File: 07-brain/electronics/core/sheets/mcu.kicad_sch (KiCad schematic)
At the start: 0 parts

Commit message: Added audio io to Brain
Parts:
- added U9: Pico, RPi_Pico:RPi_Pico_SMD_TH, symbol MCU_RaspberryPi_and_Boards:Pico
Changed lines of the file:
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@@
 	(generator_version "9.0")
 	(paper "A4")
+	(symbol
+		(lib_id "MCU_RaspberryPi_and_Boards:Pico")
+		(at 148.59 78.74 0)
+		(unit 1)
+		(exclude_from_sim no)
+		(in_bom yes)
+		(on_board yes)
+		(dnp no)
+		(fields_autoplaced yes)
+		(property "Reference" "U9"
+			(at 148.59 46.99 0)
+			(effects
+				(font
+					(size 1.27 1.27)
+				)
+			)
+		)
+		(property "Value" "Pico"
+			(at 148.59 49.53 0)
+			(effects
+				(font
+					(size 1.27 1.27)
+				)
+			)
+		)
+		(property "Footprint" "RPi_Pico:RPi_Pico_SMD_TH"
+			(at 148.59 78.74 90)
+			(effects
+				(font
+					(size 1.27 1.27)
+				)
+				(hide yes)
+			)
+		)
+		(property "Datasheet" ""
+			(at 148.59 78.74 0)
+			(effects
+				(font
+					(size 1.27 1.27)
+				)
+				(hide yes)
+			)
+		)
+		(property "Description" ""
+			(at 148.59 78.74 0)
+			(effects
+				(font
+					(size 1.27 1.27)
+				)
+				(hide yes)
+			)
+		)
+		(pin "4"
+		)
+		(pin "5"
+		)
+		(pin "6"
+		)
+		(pin "7"
+		)
+		(pin "8"
+		)
+		(pin "42"
+		)
+		(pin "43"
+		)
+		(pin "40"
+		)
+		(pin "39"
+		)
+		(pin "9"
+		)
+		(pin "38"
+		)
+		(pin "37"
+		)
+		(pin "36"
+		)
+		(pin "35"
+		)
+		(pin "34"
+		)
+		(pin "33"
+		)
+		(pin "32"
+		)
+		(pin "31"
+		)
+		(pin "10"
+		)
+		(pin "11"
+		)
+		(pin "12"
+		)
+		(pin "13"
+		)
+		(pin "14"
+		)
+		(pin "15"
+		)
+		(pin "16"
+		)
+		(pin "17"
+		)
+		(pin "18"
+		)
+		(pin "19"
+		)
+		(pin "20"
+		)
+		(pin "41"
+		)
+		(pin "30"
+		)
+		(pin "29"
+		)
+		(pin "28"
+		)
+		(pin "27"
+		)
+		(pin "26"
+		)
+		(pin "25"
+		)
+		(pin "24"
+		)
+		(pin "23"
+		)
+		(pin "22"
+		)
+		(pin "21"
+		)
+		(pin "1"
+		)
+		(pin "2"
+		)
+		(pin "3"
+		)
+		(instances
+			(project ""
+				(path "/8e2e31f3-eed5-4de1-966c-f4162758c735/e381105c-725b-4f82-965a-3ba61dbc8b0a"
+					(reference "U9")
+					(unit 1)
+				)
+			)
+		)
+	)
 )

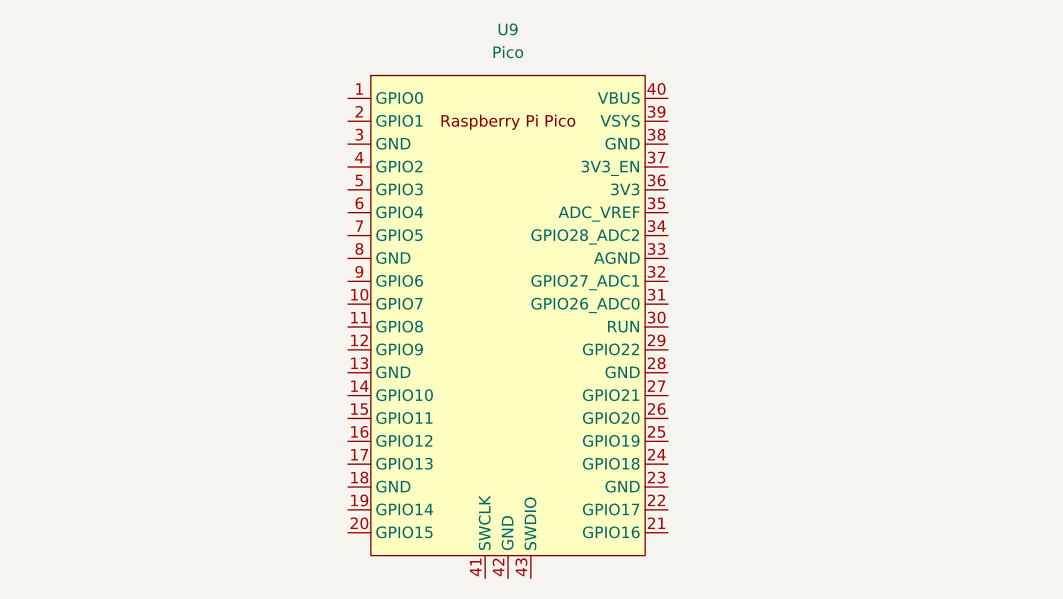
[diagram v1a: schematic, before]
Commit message: Added LED component to Brain (untested)
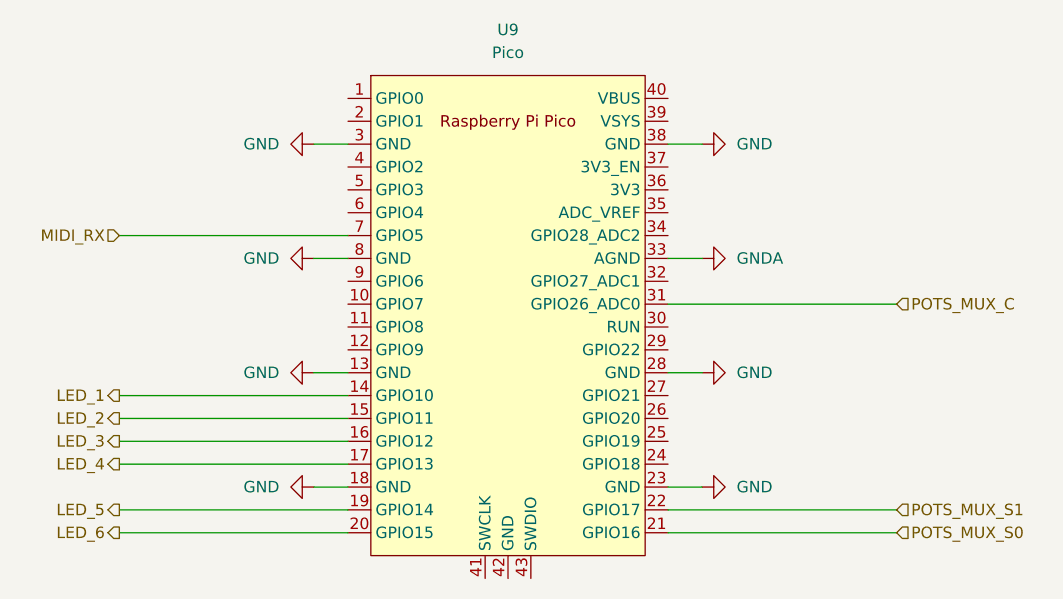
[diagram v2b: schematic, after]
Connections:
- net GND: now reaches U9.13 (GND)
- net GND: now also U9.18 (GND), U9.23 (GND), U9.28 (GND), U9.3 (GND), U9.38 (GND), U9.8 (GND)
- net LED_1: now reaches U9.14 (GPIO10)
- net LED_2: now reaches U9.15 (GPIO11)
- net LED_3: now reaches U9.16 (GPIO12)
- net LED_4: now reaches U9.17 (GPIO13)
- net LED_5: now reaches U9.19 (GPIO14)
- net LED_6: now reaches U9.20 (GPIO15)
- net POTS_MUX_S0: now reaches U9.21 (GPIO16)
- net POTS_MUX_S1: now reaches U9.22 (GPIO17)
- net POTS_MUX_C: now reaches U9.31 (GPIO26_ADC0)
- net GNDA: now reaches U9.33 (AGND)
- net MIDI_RX: now reaches U9.7 (GPIO5)

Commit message: Updated Brain schematics
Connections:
- net GND: now also U9.42 (GND)
- net MIDI_RX: now also U9.12 (GPIO9); no longer U9.7 (GPIO5)
- net UART_TX: now reaches U9.1 (GPIO0)
- net OUT_COUPLING_S2: now reaches U9.10 (GPIO7)
- net GPIO_PULSE_OUT: now reaches U9.11 (GPIO8)
- net UART_RX: now reaches U9.2 (GPIO1)
- net BTN_1: now reaches U9.24 (GPIO18)
- net BTN_2: now reaches U9.25 (GPIO19)
- net BTN_1_LED: now reaches U9.26 (GPIO20)
- net BTN_2_LED: now reaches U9.27 (GPIO21)
- net GPIO_AUDIO_IN_1: now reaches U9.32 (GPIO27_ADC1)
- net GPIO_AUDIO_IN_2: now reaches U9.34 (GPIO28_ADC2)
- net +3.3V: now reaches U9.36 (3V3)
- net +5V: now reaches U9.39 (VSYS)
- net DAC_SCK: now reaches U9.4 (GPIO2)
- net SWCLK: now reaches U9.41 (SWCLK)
- net SWDIO: now reaches U9.43 (SWDIO)
- net GPIO_PULSE_IN: now reaches U9.5 (GPIO3)
- net DAC_SDI: now reaches U9.6 (GPIO4)
- net OUT_COUPLING_S1: now reaches U9.9 (GPIO6)
- new net DAC_CS: U9.7 (GPIO5)
- no-connect marks 0 -> 5

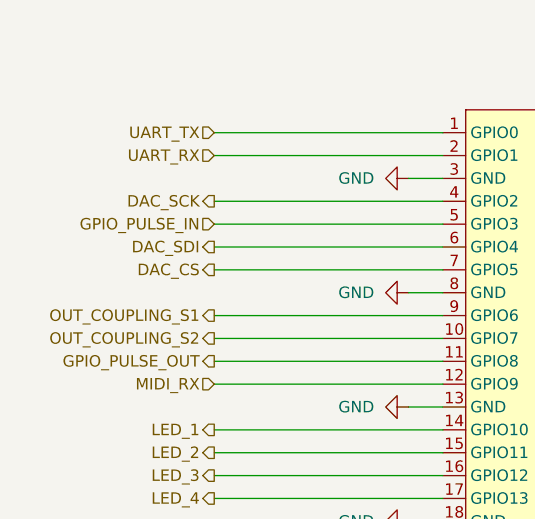
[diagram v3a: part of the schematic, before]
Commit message: Fixed DAC SPI bug in BrainSDK
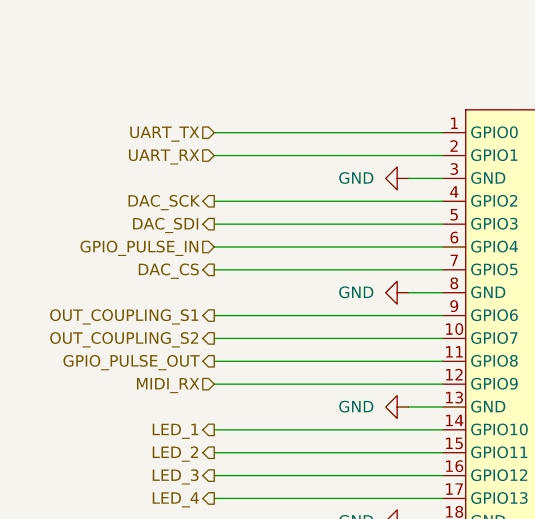
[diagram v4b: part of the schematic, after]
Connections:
- net DAC_SDI: now also U9.5 (GPIO3); no longer U9.6 (GPIO4)
- net GPIO_PULSE_IN: now also U9.6 (GPIO4); no longer U9.5 (GPIO3)
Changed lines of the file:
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@@
 	(hierarchical_label "DAC_SDI"
 		(shape output)
-		(at 105.41 67.31 180)
+		(at 105.41 64.77 180)
 		(effects
 			(font
@@
 	(hierarchical_label "GPIO_PULSE_IN"
 		(shape input)
-		(at 105.41 64.77 180)
+		(at 105.41 67.31 180)
 		(effects
 			(font

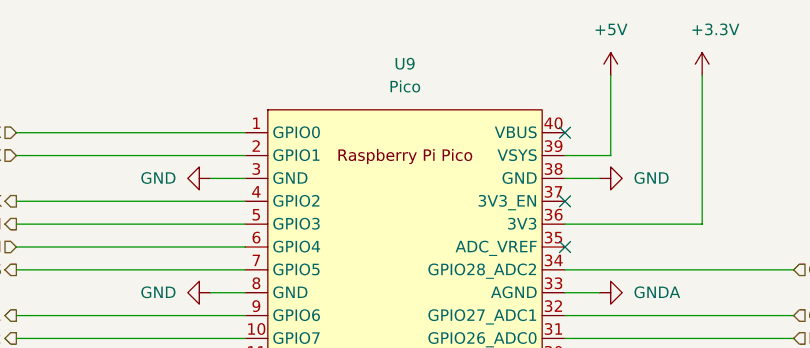
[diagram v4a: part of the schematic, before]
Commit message: Audio/CV out BrainSDK tested/working
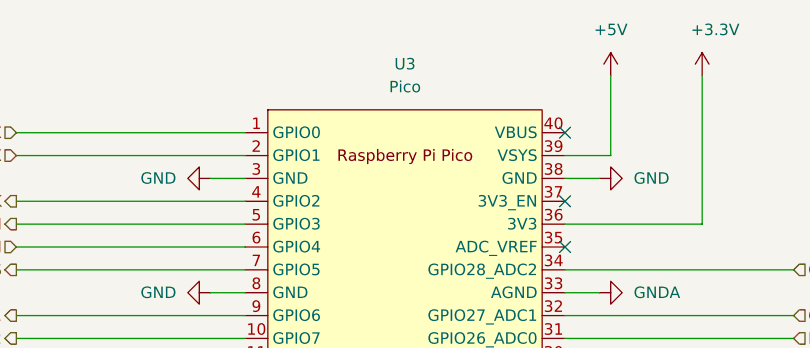
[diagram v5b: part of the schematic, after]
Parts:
- renumbered U9 to U3
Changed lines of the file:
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@@
 		(dnp no)
 		(fields_autoplaced yes)
-		(property "Reference" "#PWR080"
+		(property "Reference" "#PWR030"
 			(at 120.65 85.09 0)
 			(effects
@@
 			(project "brain-core"
 				(path "/8e2e31f3-eed5-4de1-966c-f4162758c735/e381105c-725b-4f82-965a-3ba61dbc8b0a"
-					(reference "#PWR080")
+					(reference "#PWR030")
 					(unit 1)
 				)
@@
 		(dnp no)
 		(fields_autoplaced yes)
-		(property "Reference" "#PWR079"
+		(property "Reference" "#PWR031"
 			(at 120.65 97.79 0)
 			(effects
@@
 			(project ""
 				(path "/8e2e31f3-eed5-4de1-966c-f4162758c735/e381105c-725b-4f82-965a-3ba61dbc8b0a"
-					(reference "#PWR079")
+					(reference "#PWR031")
 					(unit 1)
 				)
@@
 		(dnp no)
 		(fields_autoplaced yes)
-		(property "Reference" "#PWR083"
+		(property "Reference" "#PWR033"
 			(at 176.53 59.69 0)
 			(effects
@@
 			(project "brain-core"
 				(path "/8e2e31f3-eed5-4de1-966c-f4162758c735/e381105c-725b-4f82-965a-3ba61dbc8b0a"
-					(reference "#PWR083")
+					(reference "#PWR033")
 					(unit 1)
 				)
@@
 		(dnp no)
 		(fields_autoplaced yes)
-		(property "Reference" "#PWR082"
+		(property "Reference" "#PWR028"
 			(at 120.65 59.69 0)
 			(effects
@@
 			(project "brain-core"
 				(path "/8e2e31f3-eed5-4de1-966c-f4162758c735/e381105c-725b-4f82-965a-3ba61dbc8b0a"
-					(reference "#PWR082")
+					(reference "#PWR028")
 					(unit 1)
 				)
@@
 		(dnp no)
 		(fields_autoplaced yes)
-		(property "Reference" "#PWR081"
+		(property "Reference" "#PWR029"
 			(at 120.65 72.39 0)
 			(effects
@@
 			(project ""
 				(path "/8e2e31f3-eed5-4de1-966c-f4162758c735/e381105c-725b-4f82-965a-3ba61dbc8b0a"
-					(reference "#PWR081")
+					(reference "#PWR029")
 					(unit 1)
 				)
@@
 		(dnp no)
 		(fields_autoplaced yes)
-		(property "Reference" "#PWR076"
+		(property "Reference" "#PWR034"
 			(at 176.53 72.39 0)
 			(effects
@@
 			(project ""
 				(path "/8e2e31f3-eed5-4de1-966c-f4162758c735/e381105c-725b-4f82-965a-3ba61dbc8b0a"
-					(reference "#PWR076")
+					(reference "#PWR034")
 					(unit 1)
 				)
@@
 		(dnp no)
 		(fields_autoplaced yes)
-		(property "Reference" "U9"
+		(property "Reference" "U3"
 			(at 148.59 46.99 0)
 			(effects
@@
 			(project ""
 				(path "/8e2e31f3-eed5-4de1-966c-f4162758c735/e381105c-725b-4f82-965a-3ba61dbc8b0a"
-					(reference "U9")
+					(reference "U3")
 					(unit 1)
 				)
@@
 		(dnp no)
 		(fields_autoplaced yes)
-		(property "Reference" "#PWR077"
+		(property "Reference" "#PWR035"
 			(at 176.53 85.09 0)
 			(effects
@@
 			(project ""
 				(path "/8e2e31f3-eed5-4de1-966c-f4162758c735/e381105c-725b-4f82-965a-3ba61dbc8b0a"
-					(reference "#PWR077")
+					(reference "#PWR035")
 					(unit 1)
 				)
@@
 		(dnp no)
 		(fields_autoplaced yes)
-		(property "Reference" "#PWR031"
+		(property "Reference" "#PWR037"
 			(at 171.45 52.07 0)
 			(effects
@@
 			(project ""
 				(path "/8e2e31f3-eed5-4de1-966c-f4162758c735/e381105c-725b-4f82-965a-3ba61dbc8b0a"
-					(reference "#PWR031")
+					(reference "#PWR037")
 					(unit 1)
 				)
@@
 		(on_board yes)
 		(dnp no)
-		(property "Reference" "#PWR03"
+		(property "Reference" "#PWR038"
 			(at 181.61 52.07 0)
 			(effects
@@
 			(project ""
 				(path "/8e2e31f3-eed5-4de1-966c-f4162758c735/e381105c-725b-4f82-965a-3ba61dbc8b0a"
-					(reference "#PWR03")
+					(reference "#PWR038")
 					(unit 1)
 				)
@@
 		(dnp no)
 		(fields_autoplaced yes)
-		(property "Reference" "#PWR084"
+		(property "Reference" "#PWR032"
 			(at 148.59 123.19 0)
 			(effects
@@
 			(project ""
 				(path "/8e2e31f3-eed5-4de1-966c-f4162758c735/e381105c-725b-4f82-965a-3ba61dbc8b0a"
-					(reference "#PWR084")
+					(reference "#PWR032")
 					(unit 1)
 				)
@@
 		(dnp no)
 		(fields_autoplaced yes)
-		(property "Reference" "#PWR078"
+		(property "Reference" "#PWR036"
 			(at 176.53 97.79 0)
 			(effects
@@
 			(project "brain-core"
 				(path "/8e2e31f3-eed5-4de1-966c-f4162758c735/e381105c-725b-4f82-965a-3ba61dbc8b0a"
-					(reference "#PWR078")
-					(unit 1)
-				)
+					(reference "#PWR036")
+					(unit 1)
+				)

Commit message: Design Brain/Core PCB
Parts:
- U3: footprint RPi_Pico:RPi_Pico_SMD_TH -> Module:RaspberryPi_Pico_Common_Unspecified
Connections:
- net GND: no longer U3.42 (GND)
- net POTS_MUX_S0: now also U3.22 (GPIO17); no longer U3.21 (GPIO16)
- net POTS_MUX_S1: now also U3.21 (GPIO16); no longer U3.22 (GPIO17)
- net SWCLK: no longer names the net of U3.41 (SWCLK)
- net SWDIO: no longer names the net of U3.43 (SWDIO)
- no-connect marks 5 -> 8
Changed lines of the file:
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@@
+	)
+	(no_connect
+		(at 148.59 107.95)
 	)
 	(no_connect
@@
 		(at 166.37 80.01)
 	)
+	(no_connect
+		(at 151.13 107.95)
+	)
+	(no_connect
+		(at 146.05 107.95)
+	)
 	(wire
 		(pts
@@
 	(wire
 		(pts
-			(xy 148.59 116.84) (xy 148.59 107.95)
-		)
-		(stroke
-			(width 0)
-			(type default)
-		)
-	)
-	(wire
-		(pts
 			(xy 105.41 102.87) (xy 130.81 102.87)
 		)
@@
 		(pts
 			(xy 127 59.69) (xy 130.81 59.69)
-		)
-		(stroke
-			(width 0)
-			(type default)
-		)
-	)
-	(wire
-		(pts
-			(xy 151.13 107.95) (xy 151.13 111.76)
-		)
-		(stroke
-			(width 0)
-			(type default)
-		)
-	)
-	(wire
-		(pts
-			(xy 146.05 111.76) (xy 146.05 107.95)
 		)
 		(stroke
@@
 		)
 	)
-	(hierarchical_label "SWCLK"
-		(shape input)
-		(at 146.05 111.76 270)
-		(effects
-			(font
-				(size 1.27 1.27)
-			)
-			(justify right)
-		)
-	)
 	(hierarchical_label "BTN_2"
 		(shape input)
@@
 		)
 	)
-	(hierarchical_label "SWDIO"
-		(shape input)
-		(at 151.13 111.76 270)
-		(effects
-			(font
-				(size 1.27 1.27)
-			)
-			(justify right)
-		)
-	)
 	(hierarchical_label "LED_1"
 		(shape output)
@@
 	(hierarchical_label "POTS_MUX_S1"
 		(shape input)
-		(at 191.77 100.33 0)
+		(at 191.77 102.87 0)
 		(effects
 			(font
@@
 	(hierarchical_label "POTS_MUX_S0"
 		(shape input)
-		(at 191.77 102.87 0)
+		(at 191.77 100.33 0)
 		(effects
 			(font
@@
 			)
 		)
-		(property "Footprint" "RPi_Pico:RPi_Pico_SMD_TH"
+		(property "Footprint" "Module:RaspberryPi_Pico_Common_Unspecified"
 			(at 148.59 78.74 90)
 			(effects
@@
 		)
 		(property "Description" ""
+			(at 148.59 78.74 0)
+			(effects
+				(font
+					(size 1.27 1.27)
+				)
+				(hide yes)
+			)
+		)
+		(property "Part No." ""
+			(at 148.59 78.74 0)
+			(effects
+				(font
+					(size 1.27 1.27)
+				)
+				(hide yes)
+			)
+		)
+		(property "Part URL" ""
+			(at 148.59 78.74 0)
+			(effects
+				(font
+					(size 1.27 1.27)
+				)
+				(hide yes)
+			)
+		)
+		(property "Vendor" ""
+			(at 148.59 78.74 0)
+			(effects
+				(font
+					(size 1.27 1.27)
+				)
+				(hide yes)
+			)
+		)
+		(property "LCSC" ""
 			(at 148.59 78.74 0)
 			(effects
@@
 					(unit 1)
 				)
-			)
-		)
-	)
-	(symbol
-		(lib_id "power:GND")
-		(at 148.59 116.84 0)
-		(unit 1)
-		(exclude_from_sim no)
-		(in_bom yes)
-		(on_board yes)
-		(dnp no)
-		(fields_autoplaced yes)
-		(property "Reference" "#PWR032"
-			(at 148.59 123.19 0)
-			(effects
-				(font
-					(size 1.27 1.27)
-				)
-				(hide yes)
-			)
-		)
-		(property "Value" "GND"
-			(at 148.59 121.92 0)
-			(effects
-				(font
-					(size 1.27 1.27)
-				)
-			)
-		)
-		(property "Footprint" ""
-			(at 148.59 116.84 0)
-			(effects
-				(font
-					(size 1.27 1.27)
-				)
-				(hide yes)
-			)
-		)
-		(property "Datasheet" ""
-			(at 148.59 116.84 0)
-			(effects
-				(font
-					(size 1.27 1.27)
-				)
-				(hide yes)
-			)
-		)
-		(property "Description" "Power symbol creates a global label with name \"GND\" , ground"
-			(at 148.59 116.84 0)
-			(effects
-				(font
-					(size 1.27 1.27)
-				)
-				(hide yes)
-			)
-		)
-		(pin "1"
-		)
-		(instances
-			(project ""
-				(path "/8e2e31f3-eed5-4de1-966c-f4162758c735/e381105c-725b-4f82-965a-3ba61dbc8b0a"
-					(reference "#PWR032")
-					(unit 1)
-				)

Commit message: Brain PCB WIP
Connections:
- net GNDA is gone; now on net GND: U3.33 (AGND)
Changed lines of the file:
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@@
+	(symbol
+		(lib_id "power:GND")
+		(at 170.18 72.39 90)
+		(unit 1)
+		(exclude_from_sim no)
+		(in_bom yes)
+		(on_board yes)
+		(dnp no)
+		(fields_autoplaced yes)
+		(property "Reference" "#PWR01"
+			(at 176.53 72.39 0)
+			(effects
+				(font
+					(size 1.27 1.27)
+				)
+				(hide yes)
+			)
+		)
+		(property "Value" "GND"
+			(at 173.99 72.3899 90)
+			(effects
+				(font
+					(size 1.27 1.27)
+				)
+				(justify right)
+			)
+		)
+		(property "Footprint" ""
+			(at 170.18 72.39 0)
+			(effects
+				(font
+					(size 1.27 1.27)
+				)
+				(hide yes)
+			)
+		)
+		(property "Datasheet" ""
+			(at 170.18 72.39 0)
+			(effects
+				(font
+					(size 1.27 1.27)
+				)
+				(hide yes)
+			)
+		)
+		(property "Description" "Power symbol creates a global label with name \"GND\" , ground"
+			(at 170.18 72.39 0)
+			(effects
+				(font
+					(size 1.27 1.27)
+				)
+				(hide yes)
+			)
+		)
+		(pin "1"
+		)
+		(instances
+			(project "brain-core"
+				(path "/8e2e31f3-eed5-4de1-966c-f4162758c735/e381105c-725b-4f82-965a-3ba61dbc8b0a"
+					(reference "#PWR01")
+					(unit 1)
+				)
+			)
+		)
+	)
 	(symbol
 		(lib_id "power:GND")
@@
 					(unit 1)
 				)
-			)
-		)
-	)
-	(symbol
-		(lib_id "power:GNDA")
-		(at 170.18 72.39 90)
-		(unit 1)
-		(exclude_from_sim no)
-		(in_bom yes)
-		(on_board yes)
-		(dnp no)
-		(fields_autoplaced yes)
-		(property "Reference" "#PWR034"
-			(at 176.53 72.39 0)
-			(effects
-				(font
-					(size 1.27 1.27)
-				)
-				(hide yes)
-			)
-		)
-		(property "Value" "GNDA"
-			(at 173.99 72.3899 90)
-			(effects
-				(font
-					(size 1.27 1.27)
-				)
-				(justify right)
-			)
-		)
-		(property "Footprint" ""
-			(at 170.18 72.39 0)
-			(effects
-				(font
-					(size 1.27 1.27)
-				)
-				(hide yes)
-			)
-		)
-		(property "Datasheet" ""
-			(at 170.18 72.39 0)
-			(effects
-				(font
-					(size 1.27 1.27)
-				)
-				(hide yes)
-			)
-		)
-		(property "Description" "Power symbol creates a global label with name \"GNDA\" , analog ground"
-			(at 170.18 72.39 0)
-			(effects
-				(font
-					(size 1.27 1.27)
-				)
-				(hide yes)
-			)
-		)
-		(pin "1"
-		)
-		(instances
-			(project ""
-				(path "/8e2e31f3-eed5-4de1-966c-f4162758c735/e381105c-725b-4f82-965a-3ba61dbc8b0a"
-					(reference "#PWR034")
-					(unit 1)
-				)
